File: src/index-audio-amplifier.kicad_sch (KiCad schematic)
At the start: 50 parts, among them J1 USB_B_Micro, Q1 DMG1012T, SW1 SW_Push, U1 RP2040, U2 RT6150B-33GQW, U3 W25Q16JVUXIQ, U4 MAX98360CENL, U5 TLV70033_SOT23-5, U6 MAX98360CENL, X1 12MHz

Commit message: Associate remaining footprints
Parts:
- C101, C102, C19, C21: footprint Capacitor_SMD:C_01005_0402Metric -> Capacitor_SMD:C_0603_1608Metric
- C20, C22: footprint Capacitor_SMD:C_01005_0402Metric -> Capacitor_SMD:C_0402_1005Metric
- D2: footprint (none) -> LED_SMD:LED_0603_1608Metric
- J1: footprint (none) -> Connector_USB:USB_Micro-B_Amphenol_10103594-0001LF_Horizontal
- L1: footprint (none) -> Inductor_SMD:L_0805_2012Metric
- SW1: footprint (none) -> Button_Switch_SMD:SW_Push_1P1T_NO_Vertical_Wuerth_434133025816
- X1: footprint (none) -> Crystal:Crystal_SMD_3225-4Pin_3.2x2.5mm
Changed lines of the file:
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@@
 			)
 		)
-		(property "Footprint" ""
+		(property "Footprint" "Inductor_SMD:L_0805_2012Metric"
 			(at 97.79 43.18 0)
 			(effects
@@
 			)
 		)
-		(property "Footprint" ""
+		(property "Footprint" "LED_SMD:LED_0603_1608Metric"
 			(at 165.1 139.7 0)
 			(effects
@@
 			)
 		)
-		(property "Footprint" ""
+		(property "Footprint" "Button_Switch_SMD:SW_Push_1P1T_NO_Vertical_Wuerth_434133025816"
 			(at 49.53 76.2 0)
 			(effects
@@
 			)
 		)
-		(property "Footprint" "Capacitor_SMD:C_01005_0402Metric"
+		(property "Footprint" "Capacitor_SMD:C_0603_1608Metric"
 			(at 178.7652 110.49 0)
 			(effects
@@
 			)
 		)
-		(property "Footprint" ""
+		(property "Footprint" "Connector_USB:USB_Micro-B_Amphenol_10103594-0001LF_Horizontal"
 			(at 39.37 35.56 0)
 			(effects
@@
 			)
 		)
-		(property "Footprint" "Capacitor_SMD:C_01005_0402Metric"
+		(property "Footprint" "Capacitor_SMD:C_0402_1005Metric"
 			(at 230.8352 110.49 0)
 			(effects
@@
 			)
 		)
-		(property "Footprint" "Capacitor_SMD:C_01005_0402Metric"
+		(property "Footprint" "Capacitor_SMD:C_0603_1608Metric"
 			(at 201.6252 110.49 0)
 			(effects
@@
 			)
 		)
-		(property "Footprint" "Capacitor_SMD:C_01005_0402Metric"
+		(property "Footprint" "Capacitor_SMD:C_0603_1608Metric"
 			(at 223.2152 110.49 0)
 			(effects
@@
 			)
 		)
-		(property "Footprint" "Capacitor_SMD:C_01005_0402Metric"
+		(property "Footprint" "Capacitor_SMD:C_0603_1608Metric"
 			(at 223.2152 149.86 0)
 			(effects
@@
 			)
 		)
-		(property "Footprint" ""
+		(property "Footprint" "Crystal:Crystal_SMD_3225-4Pin_3.2x2.5mm"
 			(at 55.88 132.08 0)
 			(effects
@@
 			)
 		)
-		(property "Footprint" "Capacitor_SMD:C_01005_0402Metric"
+		(property "Footprint" "Capacitor_SMD:C_0402_1005Metric"
 			(at 230.8352 149.86 0)
 			(effects

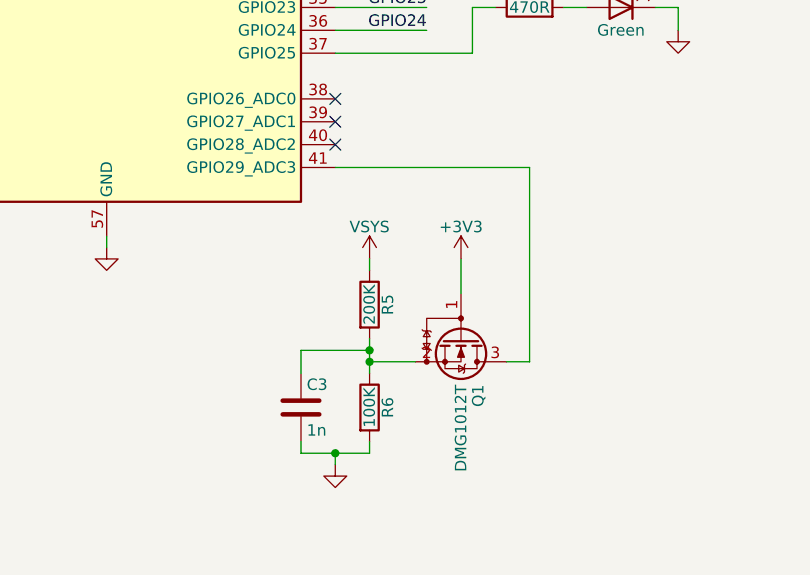
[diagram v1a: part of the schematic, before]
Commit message: Remove unused analogue VSYS monitor (GPIO29)
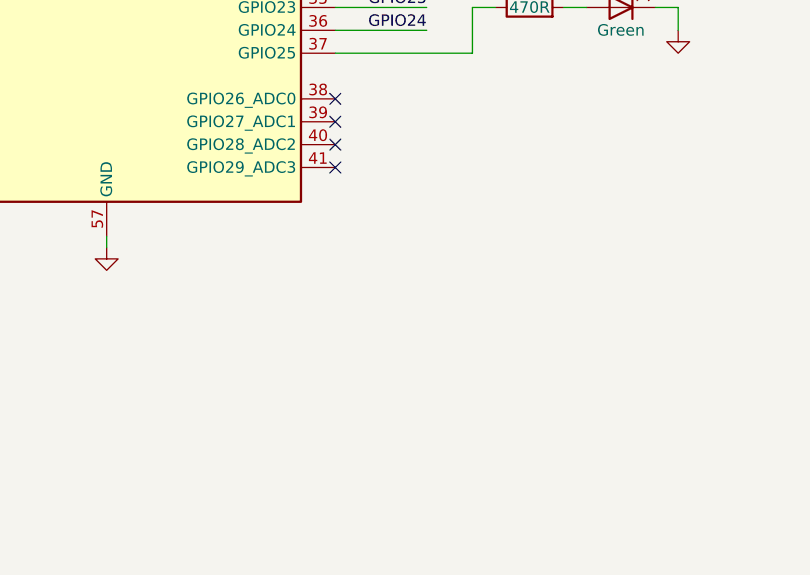
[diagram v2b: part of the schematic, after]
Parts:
- removed C3: 1n, Capacitor_SMD:C_0603_1608Metric, symbol Device:C
- removed Q1: DMG1012T, Package_TO_SOT_SMD:SOT-523, symbol Transistor_FET:DMG1012T
- removed R5: 200K, Resistor_SMD:R_0402_1005Metric, symbol Device:R
- removed R6: 100K, Resistor_SMD:R_0402_1005Metric, symbol Device:R
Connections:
- no-connect marks 24 -> 25

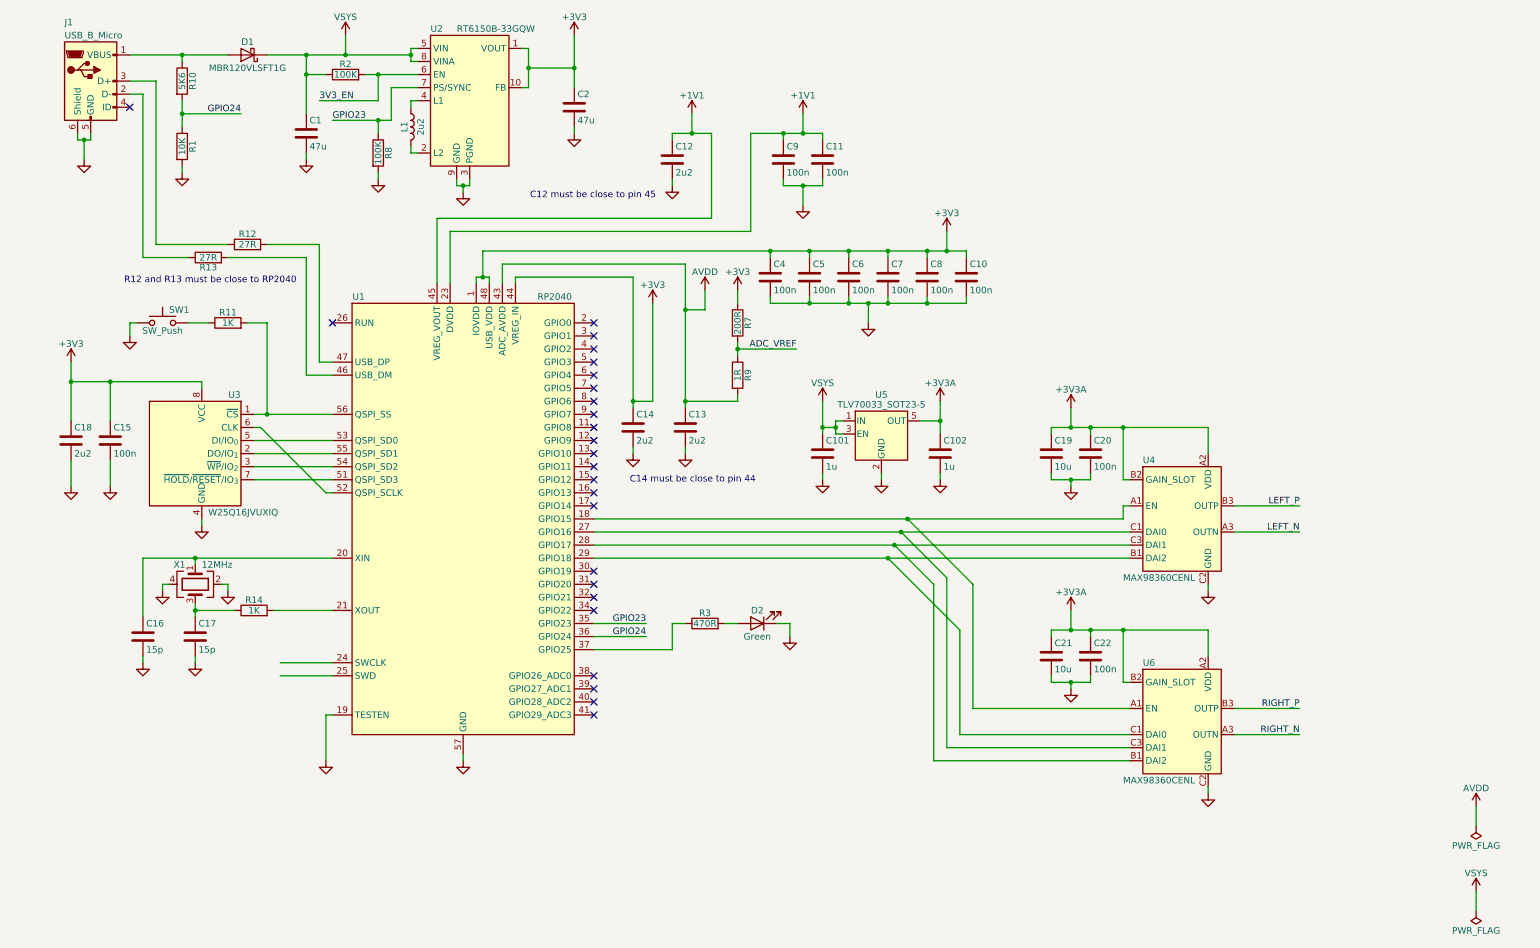
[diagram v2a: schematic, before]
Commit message: Remove external analogue reference
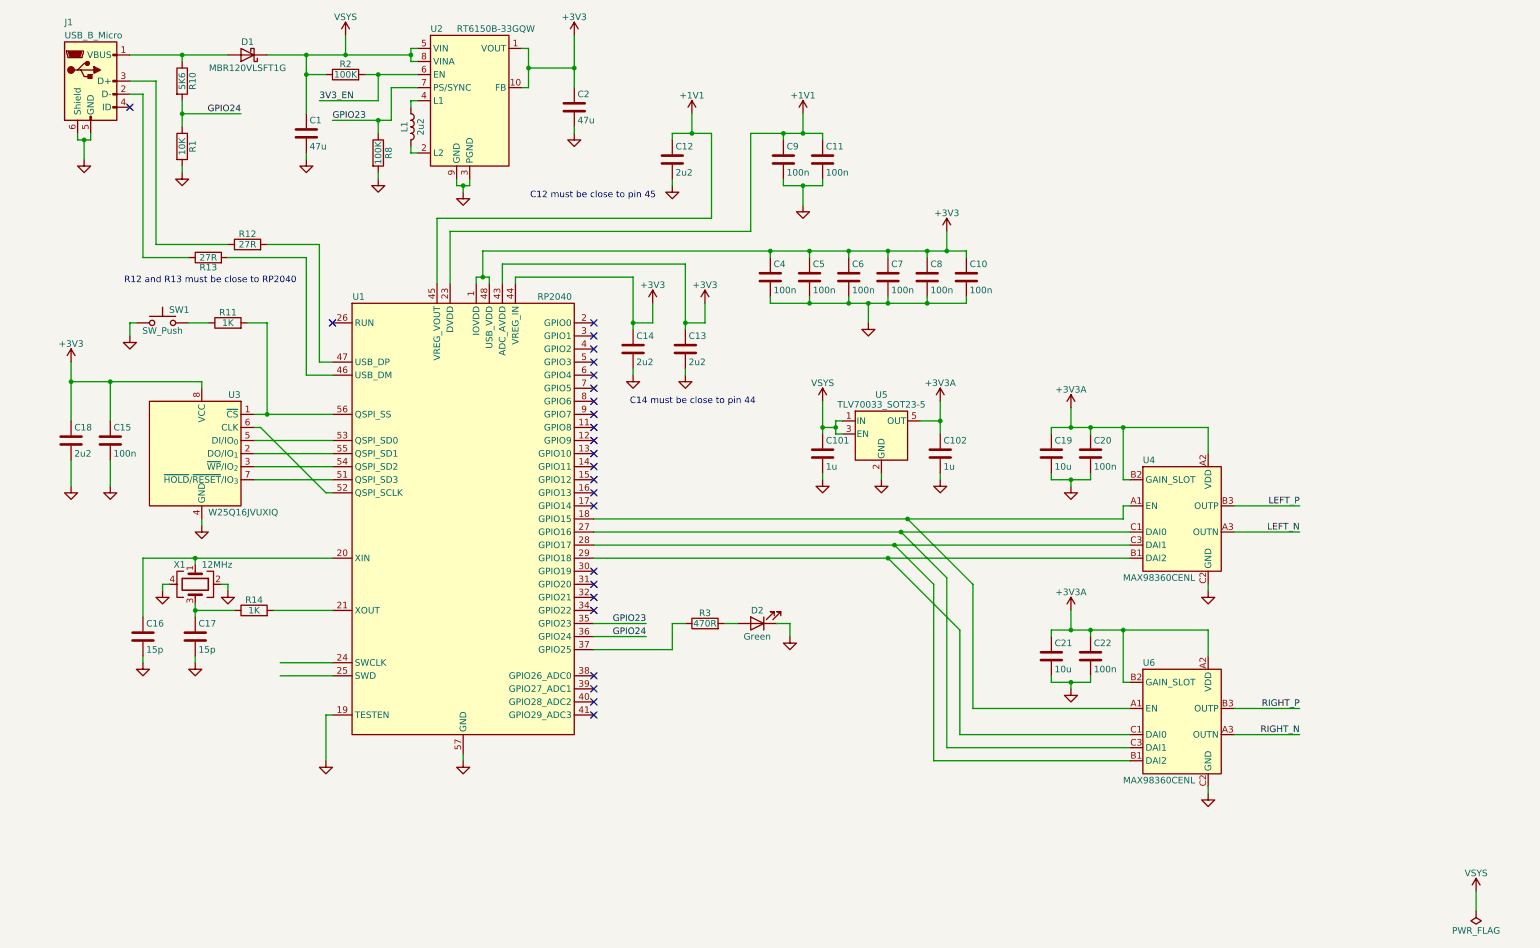
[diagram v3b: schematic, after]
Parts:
- removed R7: 200R, Resistor_SMD:R_0603_1608Metric, symbol Device:R
- removed R9: 1R, Resistor_SMD:R_0402_1005Metric, symbol Device:R
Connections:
- net AVDD is gone; now on net +3V3: C13.1, U1.43 (ADC_AVDD)
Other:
- moved on the sheet: C13, C14

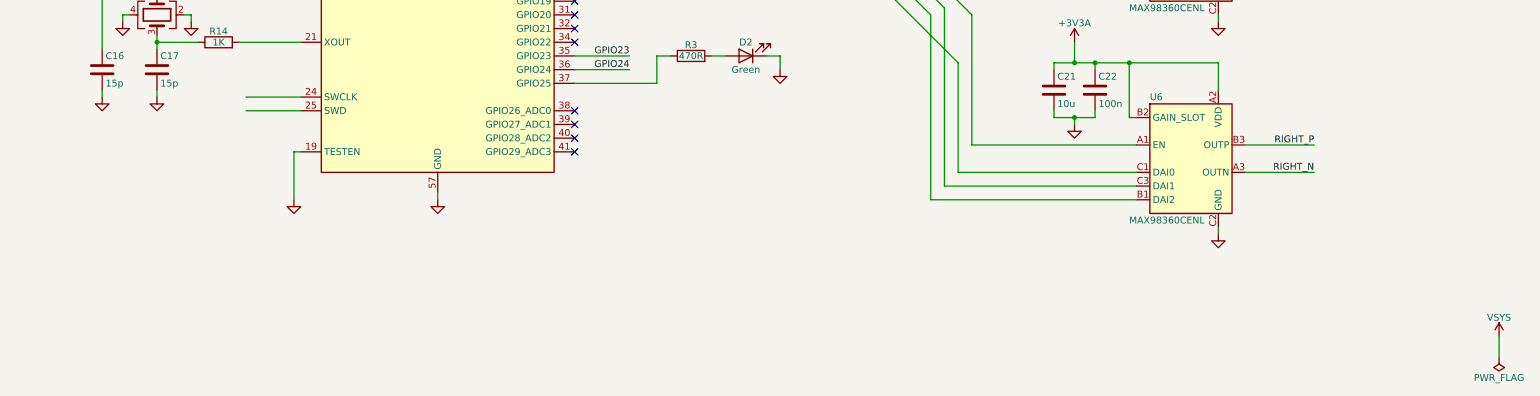
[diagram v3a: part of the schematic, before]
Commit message: Add debug interface
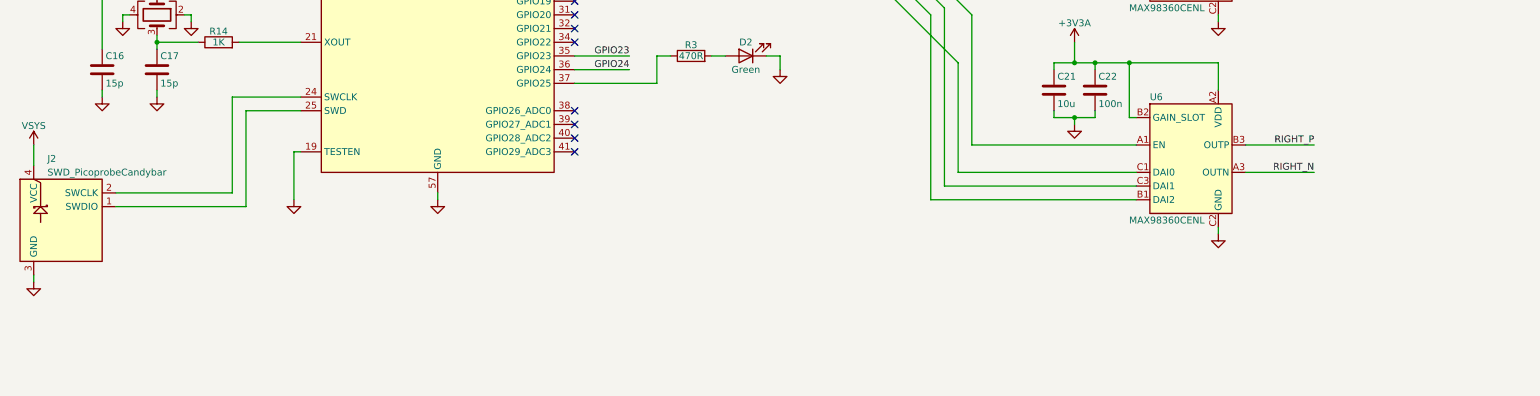
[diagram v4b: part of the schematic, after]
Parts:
- added J2: SWD_PicoprobeCandybar, Connector_PicoprobeCandybar:SWD_PicoprobeCandybar_PressFit_Compact, symbol Connector_PicoprobeCandybar:SWD_PicoprobeCandybar
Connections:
- net GND: now also J2.3 (GND)
- net VSYS: now also J2.4 (VCC)
- net at U1.24 (SWCLK): now also J2.2 (SWCLK)
- net at U1.25 (SWD): now also J2.1 (SWDIO)
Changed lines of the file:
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@@
 	(wire
 		(pts
-			(xy 304.8 191.77) (xy 304.8 195.58)
+			(xy 69.85 165.1) (xy 69.85 147.32)
 		)
 		(stroke
@@
 	(wire
 		(pts
+			(xy 33.02 156.21) (xy 33.02 160.02)
+		)
+		(stroke
+			(width 0)
+			(type default)
+		)
+	)
+	(wire
+		(pts
 			(xy 175.26 67.31) (xy 182.88 67.31)
 		)
@@
 	(wire
 		(pts
+			(xy 72.39 149.86) (xy 72.39 167.64)
+		)
+		(stroke
+			(width 0)
+			(type default)
+		)
+	)
+	(wire
+		(pts
 			(xy 69.85 29.21) (xy 77.47 29.21)
 		)
@@
 	(wire
 		(pts
+			(xy 33.02 181.61) (xy 33.02 180.34)
+		)
+		(stroke
+			(width 0)
+			(type default)
+		)
+	)
+	(wire
+		(pts
 			(xy 57.15 92.71) (xy 57.15 93.98)
 		)
@@
 	(wire
 		(pts
+			(xy 72.39 167.64) (xy 48.26 167.64)
+		)
+		(stroke
+			(width 0)
+			(type default)
+		)
+	)
+	(wire
+		(pts
 			(xy 97.79 38.1) (xy 97.79 39.37)
 		)
@@
 	(wire
 		(pts
+			(xy 69.85 147.32) (xy 82.55 147.32)
+		)
+		(stroke
+			(width 0)
+			(type default)
+		)
+	)
+	(wire
+		(pts
 			(xy 237.49 163.83) (xy 201.93 163.83)
 		)
@@
 	(wire
 		(pts
-			(xy 49.53 132.08) (xy 49.53 133.35)
+			(xy 48.26 165.1) (xy 69.85 165.1)
 		)
 		(stroke
@@
 	(wire
 		(pts
-			(xy 97.79 46.99) (xy 97.79 48.26)
+			(xy 49.53 132.08) (xy 49.53 133.35)
 		)
 		(stroke
@@
 	(wire
 		(pts
-			(xy 152.4 40.64) (xy 152.4 44.45)
+			(xy 97.79 46.99) (xy 97.79 48.26)
 		)
 		(stroke
@@
 	(wire
 		(pts
-			(xy 72.39 147.32) (xy 82.55 147.32)
+			(xy 152.4 40.64) (xy 152.4 44.45)
 		)
 		(stroke
@@
 	)
 	(symbol
-		(lib_id "power:VCC")
-		(at 304.8 191.77 0)
-		(unit 1)
-		(exclude_from_sim no)
-		(in_bom yes)
-		(on_board yes)
-		(dnp no)
-		(property "Reference" "#PWR035"
-			(at 304.8 195.58 0)
-			(effects
-				(font
-					(size 1.27 1.27)
-				)
-				(hide yes)
-			)
-		)
-		(property "Value" "VSYS"
-			(at 304.8 188.214 0)
-			(effects
-				(font
-					(size 1.27 1.27)
-				)
-			)
-		)
-		(property "Footprint" ""
-			(at 304.8 191.77 0)
-			(effects
-				(font
-					(size 1.27 1.27)
-				)
-				(hide yes)
-			)
-		)
-		(property "Datasheet" ""
-			(at 304.8 191.77 0)
-			(effects
-				(font
-					(size 1.27 1.27)
-				)
-				(hide yes)
-			)
-		)
-		(property "Description" "Power symbol creates a global label with name \"VCC\""
-			(at 304.8 191.77 0)
-			(effects
-				(font
-					(size 1.27 1.27)
-				)
-				(hide yes)
-			)
-		)
-		(pin "1"
-		)
-		(instances
-			(project "index-audio-amplifier"
-				(path "/dc35f43b-99fc-498e-a143-7e0669c7658b"
-					(reference "#PWR035")
-					(unit 1)
-				)
-			)
-		)
-	)
-	(symbol
 		(lib_id "power:GND")
 		(at 57.15 120.65 0)
@@
 	)
 	(symbol
+		(lib_id "Connector_PicoprobeCandybar:SWD_PicoprobeCandybar")
+		(at 38.1 170.18 0)
+		(unit 1)
+		(exclude_from_sim no)
+		(in_bom no)
+		(on_board yes)
+		(dnp no)
+		(property "Reference" "J2"
+			(at 35.56 158.75 0)
+			(effects
+				(font
+					(size 1.27 1.27)
+				)
+				(justify left)
+			)
+		)
+		(property "Value" "SWD_PicoprobeCandybar"
+			(at 35.56 161.29 0)
+			(effects
+				(font
+					(size 1.27 1.27)
+				)
+				(justify left)
+			)
+		)
+		(property "Footprint" "Connector_PicoprobeCandybar:SWD_PicoprobeCandybar_PressFit_Compact"
+			(at 38.1 193.04 0)
+			(effects
+				(font
+					(size 1.27 1.27)
+				)
+				(hide yes)
+			)
+		)
+		(property "Datasheet" "https://gitlab.com/recursivenomad/picoprobe-candybar/"
+			(at 38.1 195.58 0)
+			(effects
+				(font
+					(size 1.27 1.27)
+				)
+				(hide yes)
+			)
+		)
+		(property "Description" "A zero-cost press-fit debug interface for the Picoprobe Candybar debug probe, providing only SWD and power"
+			(at 38.1 198.12 0)
+			(effects
+				(font
+					(size 1.27 1.27)
+				)
+				(hide yes)
+			)
+		)
+		(pin "3"
+		)
+		(pin "4"
+		)
+		(pin "1"
+		)
+		(pin "2"
+		)
+		(instances
+			(project ""
+				(path "/dc35f43b-99fc-498e-a143-7e0669c7658b"
+					(reference "J2")
+					(unit 1)
+				)
+			)
+		)
+	)
+	(symbol
 		(lib_id "power:GND")
 		(at 107.95 55.88 0)
@@
 	)
 	(symbol
-		(lib_id "power:PWR_FLAG")
-		(at 304.8 195.58 180)
+		(lib_id "Device:C")
+		(at 177.8 106.68 0)
 		(unit 1)
 		(exclude_from_sim no)
@@
 		(on_board yes)
 		(dnp no)
-		(property "Reference" "#FLG01"
-			(at 304.8 197.485 0)
+		(property "Reference" "C101"
+			(at 178.435 104.14 0)
 			(effects
 				(font
 					(size 1.27 1.27)
 				)
-				(hide yes)
+				(justify left)
 			)
 		)
-		(property "Value" "PWR_FLAG"
-			(at 304.8 199.39 0)
+		(property "Value" "1u"
+			(at 178.435 109.22 0)
 			(effects
 				(font
 					(size 1.27 1.27)
 				)
+				(justify left)
 			)
 		)
-		(property "Footprint" ""
-			(at 304.8 195.58 0)
+		(property "Footprint" "Capacitor_SMD:C_0603_1608Metric"
+			(at 178.7652 110.49 0)
 			(effects
 				(font
@@
 		)
 		(property "Datasheet" "~"
-			(at 304.8 195.58 0)
+			(at 177.8 106.68 0)
 			(effects
 				(font
@@
 			)
 		)
-		(property "Description" "Special symbol for telling ERC where power comes from"
-			(at 304.8 195.58 0)
+		(property "Description" "Unpolarized capacitor"
+			(at 177.8 106.68 0)
 			(effects
 				(font
@@
 			)
 		)
+		(pin "2"
+		)
 		(pin "1"
 		)
 		(instances
-			(project ""
+			(project "index-audio-amplifier"
 				(path "/dc35f43b-99fc-498e-a143-7e0669c7658b"
-					(reference "#FLG01")
+					(reference "C101")
 					(unit 1)
 				)
@@
 	)
 	(symbol
-		(lib_id "Device:C")
-		(at 177.8 106.68 0)
+		(lib_id "power:GND")
+		(at 33.02 181.61 0)
 		(unit 1)
 		(exclude_from_sim no)
@@
 		(on_board yes)
 		(dnp no)
-		(property "Reference" "C101"
-			(at 178.435 104.14 0)
+		(property "Reference" "#PWR010"
+			(at 33.02 187.96 0)
 			(effects
 				(font
 					(size 1.27 1.27)
 				)
-				(justify left)
+				(hide yes)
 			)
 		)
-		(property "Value" "1u"
-			(at 178.435 109.22 0)
+		(property "Value" "GND"
+			(at 33.02 185.42 0)
 			(effects
 				(font
 					(size 1.27 1.27)
 				)
-				(justify left)
+				(hide yes)
 			)
 		)
-		(property "Footprint" "Capacitor_SMD:C_0603_1608Metric"
-			(at 178.7652 110.49 0)
+		(property "Footprint" ""
+			(at 33.02 181.61 0)
 			(effects
 				(font
@@
 			)
 		)
-		(property "Datasheet" "~"
-			(at 177.8 106.68 0)
+		(property "Datasheet" ""
+			(at 33.02 181.61 0)
 			(effects
 				(font
@@
 			)
 		)
-		(property "Description" "Unpolarized capacitor"
-			(at 177.8 106.68 0)
+		(property "Description" "Power symbol creates a global label with name \"GND\" , ground"
+			(at 33.02 181.61 0)
 			(effects
 				(font
@@
 			)
 		)
-		(pin "2"
-		)
 		(pin "1"
 		)
@@
 			(project "index-audio-amplifier"
 				(path "/dc35f43b-99fc-498e-a143-7e0669c7658b"
-					(reference "C101")
+					(reference "#PWR010")
 					(unit 1)
 				)
@@
 					(unit 1)
 				)
+			)
+		)
+	)
+	(symbol
+		(lib_id "power:VCC")
+		(at 33.02 156.21 0)
+		(unit 1)
+		(exclude_from_sim no)
+		(in_bom yes)
+		(on_board yes)
+		(dnp no)
+		(property "Reference" "#PWR022"
+			(at 33.02 160.02 0)
+			(effects
+				(font
+					(size 1.27 1.27)
+				)
+				(hide yes)
+			)
+		)
+		(property "Value" "VSYS"
+			(at 33.02 152.654 0)
+			(effects
+				(font
+					(size 1.27 1.27)
+				)
+			)
+		)
+		(property "Footprint" ""
+			(at 33.02 156.21 0)
+			(effects
+				(font
+					(size 1.27 1.27)
+				)
+				(hide yes)
+			)
+		)
+		(property "Datasheet" ""
+			(at 33.02 156.21 0)
+			(effects
+				(font
+					(size 1.27 1.27)
+				)
+				(hide yes)
+			)
+		)
+		(property "Description" "Power symbol creates a global label with name \"VCC\""
+			(at 33.02 156.21 0)
+			(effects
+				(font
+					(size 1.27 1.27)
+				)
+				(hide yes)
+			)
+		)
+		(pin "1"
+		)
+		(instances
+			(project "index-audio-amplifier"
+				(path "/dc35f43b-99fc-498e-a143-7e0669c7658b"
+					(reference "#PWR022")
+					(unit 1)
+				)
